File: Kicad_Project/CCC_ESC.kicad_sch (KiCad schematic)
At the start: 225 parts, among them J1 Conn_01x07, J2 Conn_01x06, J3 Conn_01x06, J4 Conn_01x06, SW1 Conn_01x02, U1 NCP5183 / TF2190-TAH, U2 NCP5183 / TF2190-TAH, U3 NCP5183 / TF2190-TAH, U4 NCS20034DR2G, U5 STM32F401CCU6_Balckpill, U6 PQDE6W-Q110 / RD5-110S12W, U7 TO220_replacement_module

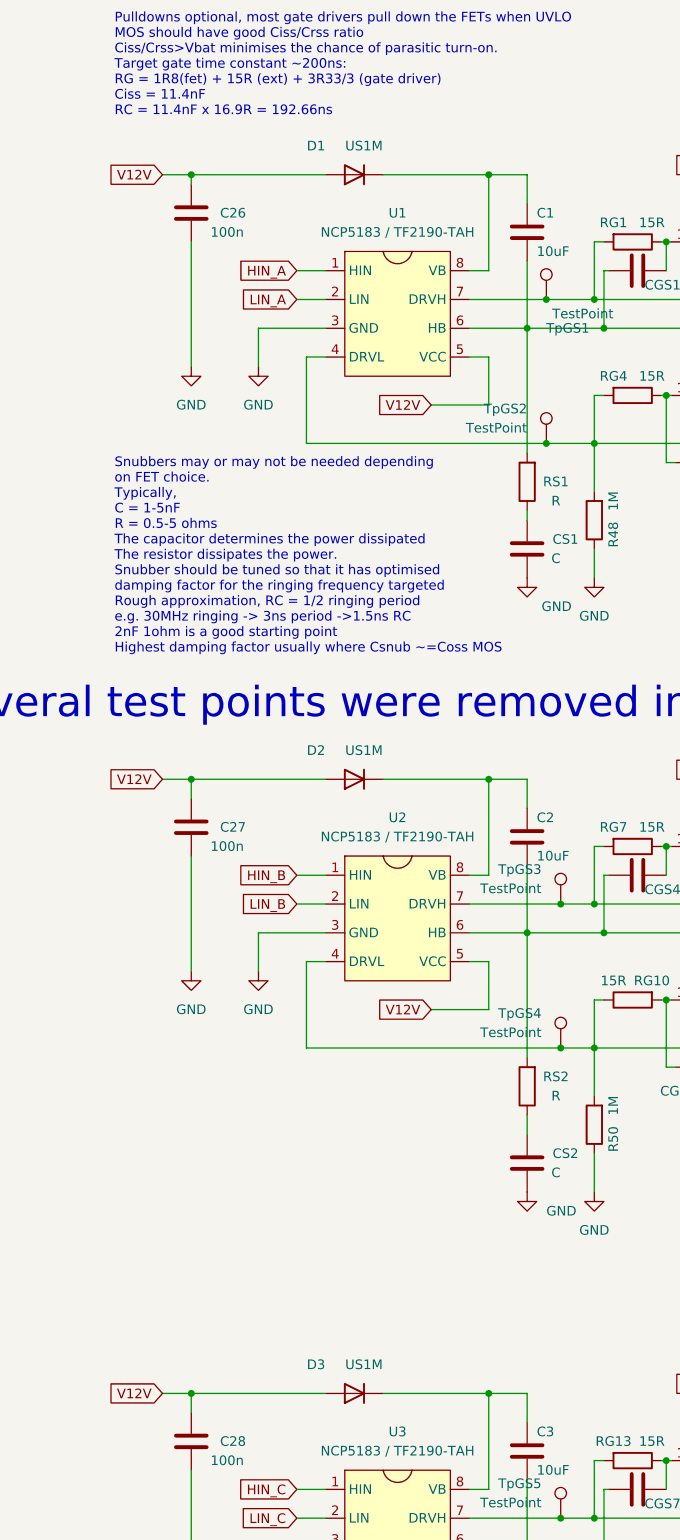
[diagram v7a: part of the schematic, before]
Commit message: added bootstrap resistors
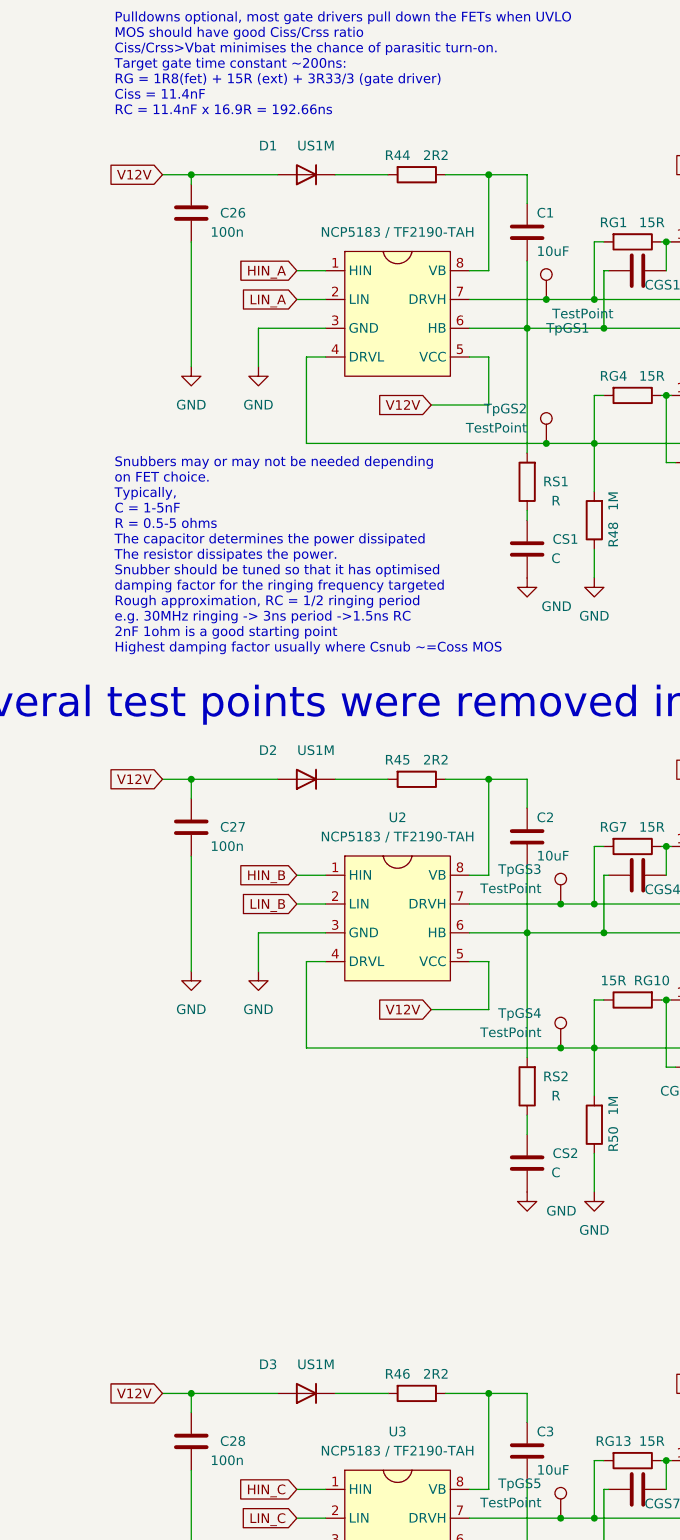
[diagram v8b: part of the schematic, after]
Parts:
- added R44, R45, R46: 2R2, Resistor_SMD:R_0603_1608Metric, symbol Device:R
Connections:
- net at C3.1, U3.8 (VB): now also R46.1; no longer D3.1 (K)
- net at C1.1, U1.8 (VB): now also R44.1; no longer D1.1 (K)
- net at C2.1, U2.8 (VB): now also R45.1; no longer D2.1 (K)
- new net: D3.1 (K), R46.2
- new net: D2.1 (K), R45.2
- new net: D1.1 (K), R44.2
